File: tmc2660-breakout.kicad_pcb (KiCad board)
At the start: 2 copper layers, 26.9 x 31.1 mm, 19 parts, among them P1 SPI, P2 StepDir, P3 Motor, P4 VCC, P5 VMOT, U1 TMC2660

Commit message: o Turn around VCC/GND connector so that it has the same direction   as the VMOT connector. Less possibly dangerous confusion ...
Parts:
- REF**: value Symbol_OSHW-Logo_SilkScreen -> OSHW
- moved P4 2.54 mm to (118.9, 42.7), turned to 180 degrees
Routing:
- net GND: track 110.4 -> 103.4 mm
- net Net-(C6-Pad1): track 13.2 -> 14.3 mm
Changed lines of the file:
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@@
     (thickness 1.6)
     (drawings 13)
-    (tracks 323)
+    (tracks 320)
     (zones 0)
     (modules 19)
@@
     (tags "LED 0805 SMD")
     (attr smd)
-    (fp_text reference D1 (at -2.921 0) (layer F.SilkS)
+    (fp_text reference D1 (at -2.286 0.635) (layer F.SilkS)
       (effects (font (size 1 1) (thickness 0.15)))
     )
@@
       (effects (font (size 1 1) (thickness 0.15)))
     )
-    (fp_text value Motor (at 1.524 11.43 180) (layer F.SilkS)
+    (fp_text value Motor (at -2.54 0.381 360) (layer F.SilkS)
       (effects (font (size 1 1) (thickness 0.15)))
     )
@@
   )
   (module Pin_Headers:Pin_Header_Straight_1x02 (layer F.Cu)
-    (at 118.872 40.132)
+    (at 118.872 42.672 180)
     (descr "Through hole pin header")
     (tags "pin header")
-    (fp_text reference P4 (at 0 -5.1) (layer F.SilkS) hide
-      (effects (font (size 1 1) (thickness 0.15)))
-    )
-    (fp_text value VCC (at 3.048 3.048) (layer F.SilkS)
-      (effects (font (size 0.8 0.8) (thickness 0.15)))
-    )
-    (fp_line (start 1.27 1.27) (end 1.27 3.81) (layer F.SilkS) (width 0.15))
-    (fp_line (start 1.55 -1.55) (end 1.55 0) (layer F.SilkS) (width 0.15))
-    (fp_line (start -1.75 -1.75) (end -1.75 4.3) (layer F.CrtYd) (width 0.05))
-    (fp_line (start 1.75 -1.75) (end 1.75 4.3) (layer F.CrtYd) (width 0.05))
-    (fp_line (start -1.75 -1.75) (end 1.75 -1.75) (layer F.CrtYd) (width 0.05))
-    (fp_line (start -1.75 4.3) (end 1.75 4.3) (layer F.CrtYd) (width 0.05))
-    (fp_line (start 1.27 1.27) (end -1.27 1.27) (layer F.SilkS) (width 0.15))
-    (fp_line (start -1.55 0) (end -1.55 -1.55) (layer F.SilkS) (width 0.15))
-    (fp_line (start -1.55 -1.55) (end 1.55 -1.55) (layer F.SilkS) (width 0.15))
-    (fp_line (start -1.27 1.27) (end -1.27 3.81) (layer F.SilkS) (width 0.15))
-    (fp_line (start -1.27 3.81) (end 1.27 3.81) (layer F.SilkS) (width 0.15))
-    (pad 1 thru_hole rect (at 0 0) (size 2.032 2.032) (drill 1.016) (layers *.Cu *.Mask F.SilkS)
-      (net 7 GND))
-    (pad 2 thru_hole oval (at 0 2.54) (size 2.032 2.032) (drill 1.016) (layers *.Cu *.Mask F.SilkS)
-      (net 21 "Net-(C6-Pad1)"))
-    (model Pin_Headers.3dshapes/Pin_Header_Straight_1x02.wrl
-      (at (xyz 0 -0.05 0))
-      (scale (xyz 1 1 1))
-      (rotate (xyz 0 0 90))
-    )
-  )
-  (module Pin_Headers:Pin_Header_Straight_1x02 (layer F.Cu)
-    (at 140.716 44.2595 180)
-    (descr "Through hole pin header")
-    (tags "pin header")
-    (fp_text reference P5 (at -0.508 -2.7305 180) (layer F.SilkS) hide
-      (effects (font (size 1 1) (thickness 0.15)))
-    )
-    (fp_text value VMOT (at 3.302 3.1115 180) (layer F.SilkS)
+    (fp_text reference P4 (at 0 -5.1 180) (layer F.SilkS) hide
+      (effects (font (size 1 1) (thickness 0.15)))
+    )
+    (fp_text value VCC (at -3.048 2.54 180) (layer F.SilkS)
       (effects (font (size 0.8 0.8) (thickness 0.15)))
     )
@@
       (net 7 GND))
     (pad 2 thru_hole oval (at 0 2.54 180) (size 2.032 2.032) (drill 1.016) (layers *.Cu *.Mask F.SilkS)
+      (net 21 "Net-(C6-Pad1)"))
+    (model Pin_Headers.3dshapes/Pin_Header_Straight_1x02.wrl
+      (at (xyz 0 -0.05 0))
+      (scale (xyz 1 1 1))
+      (rotate (xyz 0 0 90))
+    )
+  )
+  (module Pin_Headers:Pin_Header_Straight_1x02 (layer F.Cu)
+    (at 140.716 44.2595 180)
+    (descr "Through hole pin header")
+    (tags "pin header")
+    (fp_text reference P5 (at -0.508 -2.7305 180) (layer F.SilkS) hide
+      (effects (font (size 1 1) (thickness 0.15)))
+    )
+    (fp_text value VMOT (at 3.302 3.1115 180) (layer F.SilkS)
+      (effects (font (size 0.8 0.8) (thickness 0.15)))
+    )
+    (fp_line (start 1.27 1.27) (end 1.27 3.81) (layer F.SilkS) (width 0.15))
+    (fp_line (start 1.55 -1.55) (end 1.55 0) (layer F.SilkS) (width 0.15))
+    (fp_line (start -1.75 -1.75) (end -1.75 4.3) (layer F.CrtYd) (width 0.05))
+    (fp_line (start 1.75 -1.75) (end 1.75 4.3) (layer F.CrtYd) (width 0.05))
+    (fp_line (start -1.75 -1.75) (end 1.75 -1.75) (layer F.CrtYd) (width 0.05))
+    (fp_line (start -1.75 4.3) (end 1.75 4.3) (layer F.CrtYd) (width 0.05))
+    (fp_line (start 1.27 1.27) (end -1.27 1.27) (layer F.SilkS) (width 0.15))
+    (fp_line (start -1.55 0) (end -1.55 -1.55) (layer F.SilkS) (width 0.15))
+    (fp_line (start -1.55 -1.55) (end 1.55 -1.55) (layer F.SilkS) (width 0.15))
+    (fp_line (start -1.27 1.27) (end -1.27 3.81) (layer F.SilkS) (width 0.15))
+    (fp_line (start -1.27 3.81) (end 1.27 3.81) (layer F.SilkS) (width 0.15))
+    (pad 1 thru_hole rect (at 0 0 180) (size 2.032 2.032) (drill 1.016) (layers *.Cu *.Mask F.SilkS)
+      (net 7 GND))
+    (pad 2 thru_hole oval (at 0 2.54 180) (size 2.032 2.032) (drill 1.016) (layers *.Cu *.Mask F.SilkS)
       (net 9 VMot))
     (model Pin_Headers.3dshapes/Pin_Header_Straight_1x02.wrl
@@
       (effects (font (size 1 1) (thickness 0.15)))
     )
-    (fp_text value Symbol_OSHW-Logo_SilkScreen (at 0.30988 6.56082) (layer F.Fab) hide
+    (fp_text value OSHW (at 4.445 1.778 90) (layer F.Fab) hide
       (effects (font (size 1 1) (thickness 0.15)))
     )
@@
     (effects (font (size 0.8 0.8) (thickness 0.15)))
   )
-  (gr_text GND (at 121.92 40.386) (layer F.SilkS)
+  (gr_text GND (at 122.047 42.799) (layer F.SilkS)
     (effects (font (size 0.8 0.8) (thickness 0.15)))
   )
@@
   (via (at 129.794 58.547) (size 0.6) (drill 0.4) (layers F.Cu B.Cu) (net 7))
   (segment (start 124.206 44.323) (end 124.206 44.2) (width 0.25) (layer F.Cu) (net 7))
-  (segment (start 124.206 44.2) (end 120.138 40.132) (width 0.25) (layer F.Cu) (net 7))
-  (segment (start 120.138 40.132) (end 118.872 40.132) (width 0.25) (layer F.Cu) (net 7))
   (segment (start 127.617 44.323) (end 124.206 44.323) (width 0.25) (layer F.Cu) (net 7))
   (segment (start 128.889 45.72) (end 128.889 45.595) (width 0.25) (layer F.Cu) (net 7))
@@
   (segment (start 136.677 57.556) (end 137.16 58.039) (width 0.25) (layer F.Cu) (net 20))
   (via (at 137.16 58.039) (size 0.6) (drill 0.4) (layers F.Cu B.Cu) (net 20))
-  (segment (start 121.666 42.672) (end 124.714 45.72) (width 0.25) (layer F.Cu) (net 21))
-  (segment (start 124.714 45.72) (end 126.889 45.72) (width 0.25) (layer F.Cu) (net 21))
-  (segment (start 118.872 42.672) (end 121.666 42.672) (width 0.25) (layer F.Cu) (net 21))
+  (segment (start 118.872 40.132) (end 124.46 45.72) (width 0.25) (layer F.Cu) (net 21))
+  (segment (start 124.46 45.72) (end 126.889 45.72) (width 0.25) (layer F.Cu) (net 21))
   (segment (start 126.889 45.72) (end 127.3215 45.72) (width 0.25) (layer F.Cu) (net 21))
   (segment (start 127.3215 45.72) (end 129.0575 47.456) (width 0.25) (layer F.Cu) (net 21))

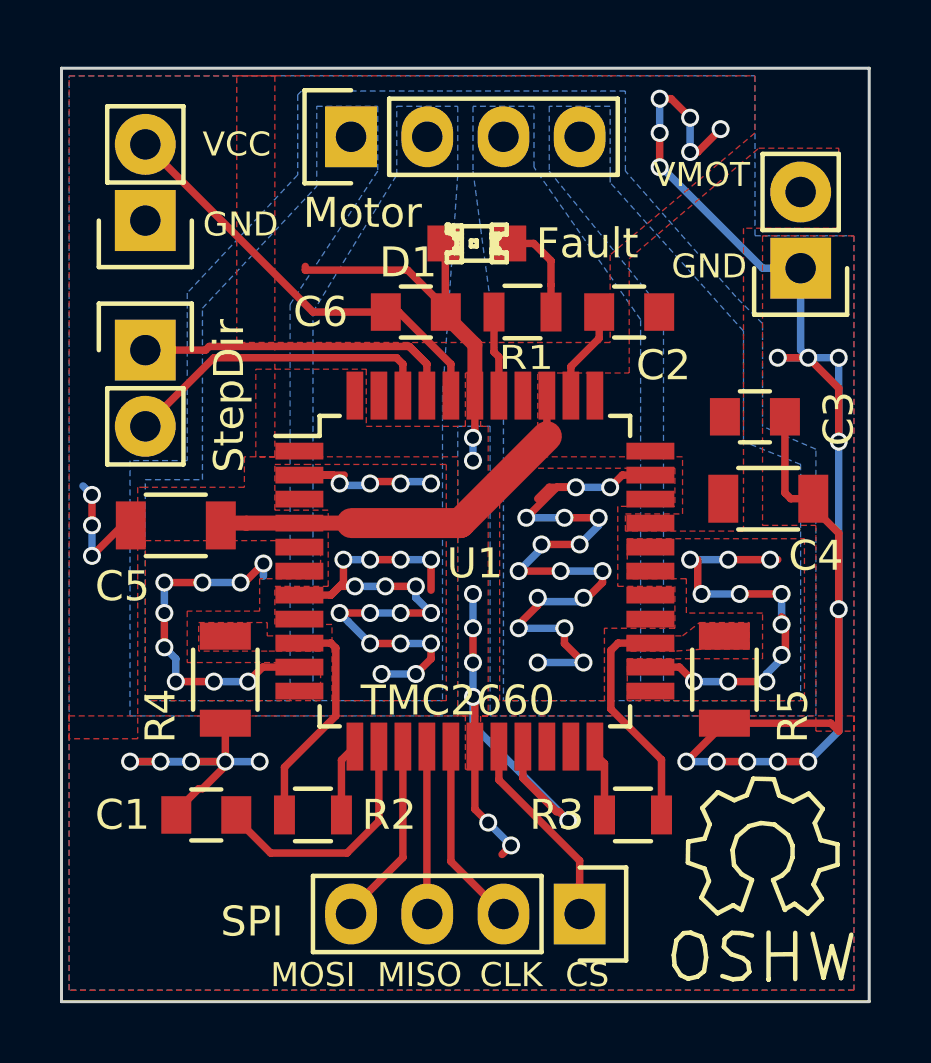
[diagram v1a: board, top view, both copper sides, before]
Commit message: o Add Fiducials.
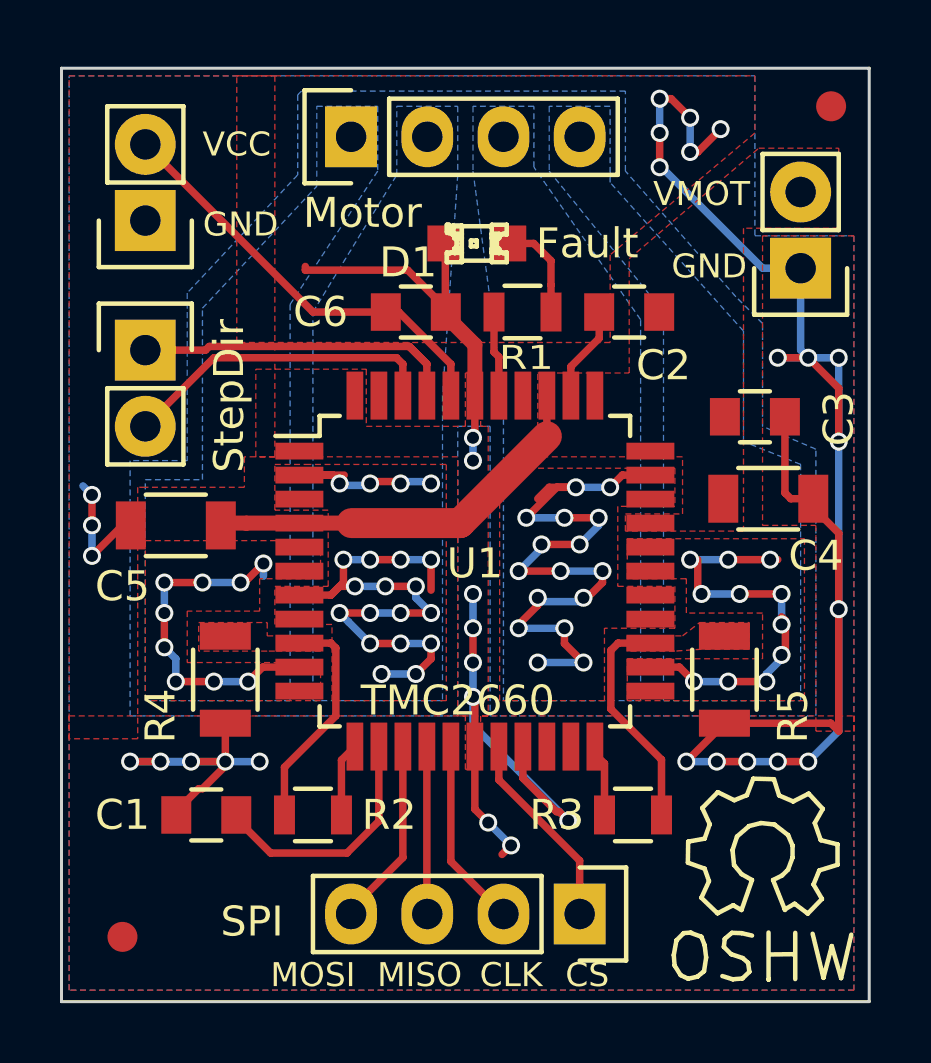
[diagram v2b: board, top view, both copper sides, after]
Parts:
- added REF**: F_topright, Fiducials:Fiducial_1mm_Dia_2.54mm_Outer_CopperTop, F.Cu at (141.7, 38.9)
- added REF**: Fiducial_bottomleft, Fiducials:Fiducial_1mm_Dia_2.54mm_Outer_CopperTop, F.Cu at (118.1, 66.5)
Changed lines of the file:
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@@
 (kicad_pcb (version 4) (host pcbnew "(2015-12-19 BZR 6385, Git 2c9e11a)-product")
   (general
-    (links 56)
+    (links 0)
     (no_connects 0)
-    (area 116.027999 37.541999 143.052001 68.757001)
+    (area 112.74 37.159999 147.476858 68.987477)
     (thickness 1.6)
     (drawings 13)
     (tracks 320)
     (zones 0)
-    (modules 19)
+    (modules 21)
     (nets 22)
   )
@@
       (effects (font (size 1 1) (thickness 0.15)))
     )
-    (fp_text value VMOT (at 3.302 3.1115 180) (layer F.SilkS)
+    (fp_text value VMOT (at 3.302 2.4765 180) (layer F.SilkS)
       (effects (font (size 0.8 0.8) (thickness 0.15)))
     )
@@
     (fp_line (start 0.35052 0.89916) (end 0.7493 1.89992) (layer F.SilkS) (width 0.15))
   )
+  (module Fiducials:Fiducial_1mm_Dia_2.54mm_Outer_CopperTop (layer F.Cu)
+    (at 141.732 38.862)
+    (descr "Circular Fiducial, 1mm bare copper top; 2.54mm keepout")
+    (tags marker)
+    (attr virtual)
+    (fp_text reference REF** (at 3.4 0.7) (layer F.SilkS) hide
+      (effects (font (size 1 1) (thickness 0.15)))
+    )
+    (fp_text value F_topright (at 2.159 2.794 90) (layer F.Fab) hide
+      (effects (font (size 1 1) (thickness 0.15)))
+    )
+    (fp_circle (center 0 0) (end 1.55 0) (layer F.CrtYd) (width 0.05))
+    (pad ~ smd circle (at 0 0) (size 1 1) (layers F.Cu F.Mask)
+      (solder_mask_margin 0.77) (clearance 0.77))
+  )
+  (module Fiducials:Fiducial_1mm_Dia_2.54mm_Outer_CopperTop (layer F.Cu)
+    (at 118.11 66.548)
+    (descr "Circular Fiducial, 1mm bare copper top; 2.54mm keepout")
+    (tags marker)
+    (attr virtual)
+    (fp_text reference REF** (at -4.318 0 90) (layer F.SilkS) hide
+      (effects (font (size 1 1) (thickness 0.15)))
+    )
+    (fp_text value Fiducial_bottomleft (at -2.921 -4.953 90) (layer F.Fab) hide
+      (effects (font (size 1 1) (thickness 0.15)))
+    )
+    (fp_circle (center 0 0) (end 1.55 0) (layer F.CrtYd) (width 0.05))
+    (pad ~ smd circle (at 0 0) (size 1 1) (layers F.Cu F.Mask)
+      (solder_mask_margin 0.77) (clearance 0.77))
+  )
   (gr_text "github.com\nhzeller/tmc2660-breakout" (at 135.128 41.402 90) (layer B.SilkS)
